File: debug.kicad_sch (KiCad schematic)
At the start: 80 parts, among them J8 USB4105-GF-A, J9 0878311420, Q10 DTC014TEBTL, Q11 DTC014TEBTL, Q12 DTC014TEBTL, U37 WE-TVS-82400152, U38 MIC5211-3.3YM6-TR, U39 93LC66BT-IMC, U40 FT4232HPQ, U41 TPD4E05U06QDQARQ1_PASS, U42 74AVC4T245RSVRG4, U43 74AVC4T245RSVRG4, U44 SN74AVC2T245RSWR, U45 SN74AVC2T245RSWR, U46 NC7WZ07P6X, Y7 ABM8G-12.000MHZ-18-D2Y-T

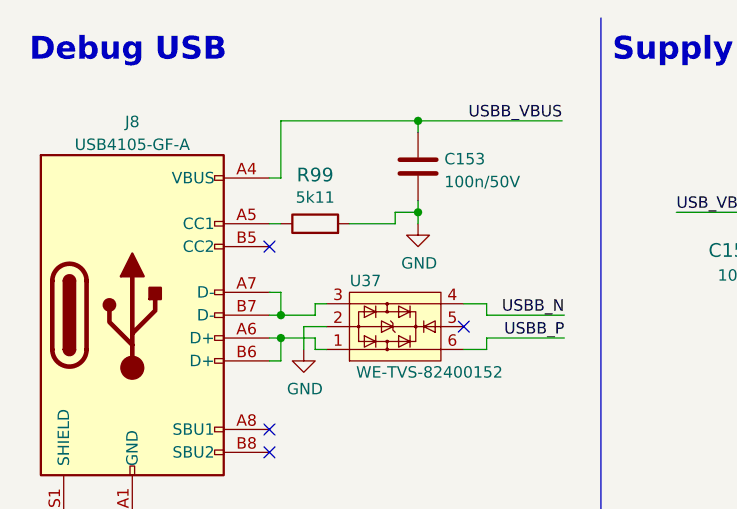
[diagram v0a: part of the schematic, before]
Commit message: Add CC2 5K1 pulldown
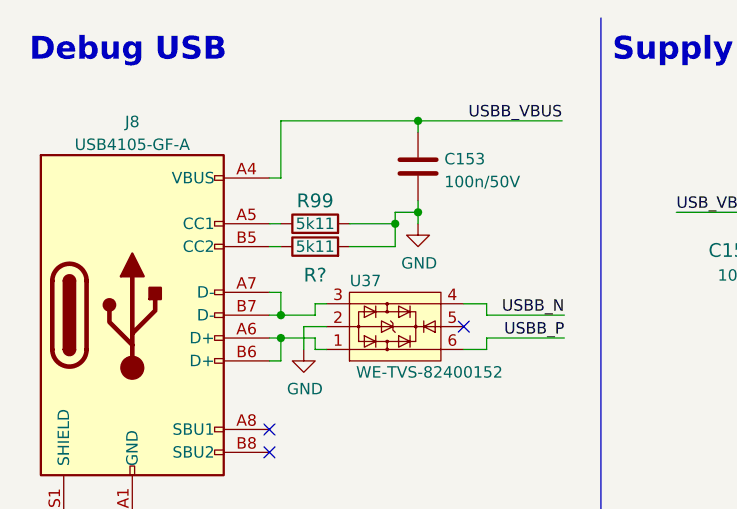
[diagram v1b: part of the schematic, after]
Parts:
- added R?: R_5k11_0402, kria-k26-devboard-footprints:0402-res, symbol kria-k26-devboard:R_5k11_0402
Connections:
- net GND: now also R?.2
- net at J8.B5 (CC2): now also R?.1
- no-connect marks 37 -> 36
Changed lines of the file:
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@@
   (junction (at 53.34 100.33) (diameter 0) (color 0 0 0 0)
   )
+  (junction (at 54.61 35.56) (diameter 0) (color 0 0 0 0)
+  )
   (junction (at 290.83 135.89) (diameter 0) (color 0 0 0 0)
   )
@@
   (no_connect (at 227.33 187.96))
   (no_connect (at 40.64 60.96))
-  (no_connect (at 40.64 38.1))
   (no_connect (at 326.39 66.04))
   (no_connect (at 227.33 149.86))
@@
     (stroke (width 0) (type default) (color 0 0 0 0))
   )
+  (wire (pts (xy 40.64 38.1) (xy 41.91 38.1))
+    (stroke (width 0) (type default) (color 0 0 0 0))
+  )
   (wire (pts (xy 40.64 101.6) (xy 40.64 100.33))
     (stroke (width 0) (type default) (color 0 0 0 0))
@@
     (stroke (width 0) (type default) (color 0 0 0 0))
   )
+  (wire (pts (xy 49.53 38.1) (xy 54.61 38.1))
+    (stroke (width 0) (type default) (color 0 0 0 0))
+  )
   (polyline (pts (xy 299.72 234.95) (xy 299.72 252.73))
     (stroke (width 0) (type default) (color 0 0 0 0))
@@
     (stroke (width 0) (type default) (color 0 0 0 0))
   )
+  (wire (pts (xy 54.61 38.1) (xy 54.61 35.56))
+    (stroke (width 0) (type default) (color 0 0 0 0))
+  )
   (wire (pts (xy 41.91 45.72) (xy 40.64 45.72))
     (stroke (width 0) (type default) (color 0 0 0 0))
@@
   (symbol (lib_id "kria-k26-devboard:R_5k11_0402") (at 45.72 35.56 0) (unit 1)
     (in_bom yes) (on_board yes)
-    (property "Reference" "R99" (id 0) (at 45.72 30.1498 0)
+    (property "Reference" "R99" (id 0) (at 45.72 33.02 0)
       (effects (font (size 1.524 1.524)))
     )
@@
       (effects (font (size 1.524 1.524)) (justify left) hide)
     )
-    (property "Val" "5k11" (id 6) (at 45.72 32.639 0))
+    (property "Val" "5k11" (id 6) (at 45.72 35.56 0))
     (pin "1")
     (pin "2")
@@
     (pin "9")
   )
+  (symbol (lib_id "kria-k26-devboard:R_5k11_0402") (at 45.72 38.1 0) (unit 1)
+    (in_bom yes) (on_board yes)
+    (property "Reference" "R?" (id 0) (at 45.72 41.275 0)
+      (effects (font (size 1.524 1.524)))
+    )
+    (property "Value" "R_5k11_0402" (id 1) (at 45.72 41.91 0)
+      (effects (font (size 1.524 1.524)) hide)
+    )
+    (property "Footprint" "kria-k26-devboard-footprints:0402-res" (id 2) (at 50.8 33.02 0)
+      (effects (font (size 1.524 1.524)) (justify left) hide)
+    )
+    (property "Datasheet" "" (id 3) (at 45.72 38.1 0)
+      (effects (font (size 1.27 1.27)) hide)
+    )
+    (property "Manufacturer" "WALSIN" (id 4) (at 50.8 27.94 0)
+      (effects (font (size 1.524 1.524)) (justify left) hide)
+    )
+    (property "MPN" "WR04X5111FTL" (id 5) (at 50.8 30.48 0)
+      (effects (font (size 1.524 1.524)) (justify left) hide)
+    )
+    (property "Val" "5k11" (id 6) (at 45.72 38.1 0))
+    (pin "1")
+    (pin "2")
+  )
 )

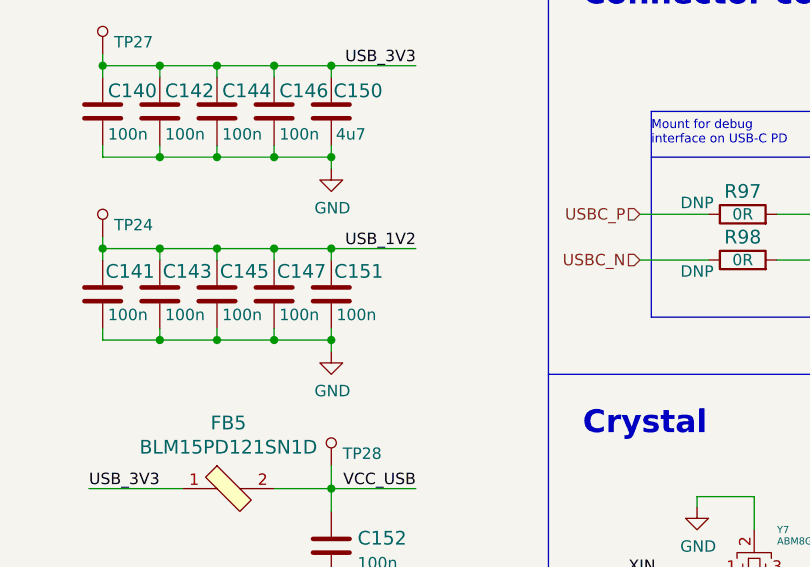
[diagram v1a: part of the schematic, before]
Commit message: Added 4u7 to FTDI Vregout
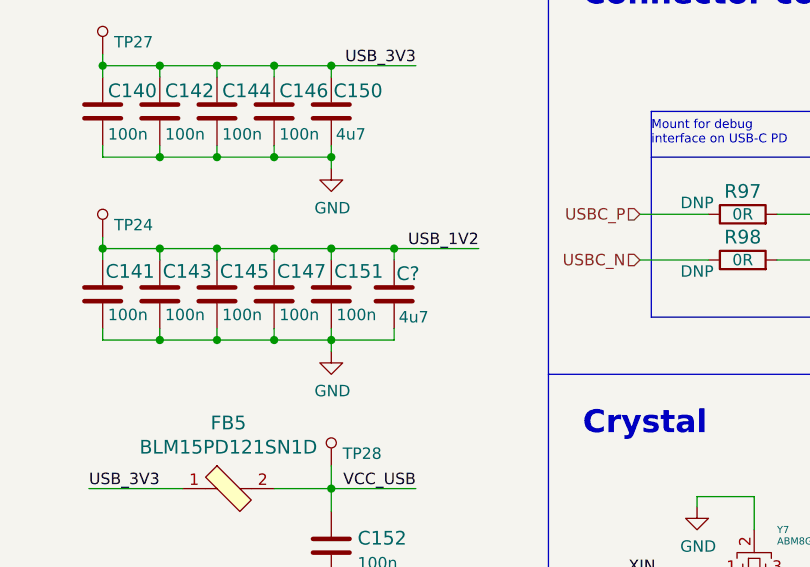
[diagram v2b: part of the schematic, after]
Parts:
- added C?: C_4u7_0402, kria-k26-devboard-footprints:0402-cap, symbol kria-k26-devboard:C_4u7_0402
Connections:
- net GND: now also C?.2
- net USB_1V2: now also C?.1
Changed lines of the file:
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@@
     (comment 2 "Antmicro Ltd.")
   )
+  (junction (at 60.325 120.65) (diameter 0) (color 0 0 0 0)
+  )
   (junction (at 131.318 261.62) (diameter 0) (color 0 0 0 0)
   )
@@
     (stroke (width 0) (type default) (color 0 0 0 0))
   )
+  (wire (pts (xy 53.34 130.81) (xy 60.325 130.81))
+    (stroke (width 0) (type default) (color 0 0 0 0))
+  )
   (wire (pts (xy 153.67 55.88) (xy 166.37 55.88))
     (stroke (width 0) (type default) (color 0 0 0 0))
@@
     (stroke (width 0) (type default) (color 0 0 0 0))
   )
-  (wire (pts (xy 62.738 120.65) (xy 53.34 120.65))
+  (wire (pts (xy 69.723 120.65) (xy 60.325 120.65))
     (stroke (width 0) (type default) (color 0 0 0 0))
   )
@@
     (stroke (width 0) (type default) (color 0 0 0 0))
   )
+  (wire (pts (xy 60.325 120.65) (xy 53.34 120.65))
+    (stroke (width 0) (type default) (color 0 0 0 0))
+  )
   (wire (pts (xy 327.66 114.3) (xy 332.74 114.3))
     (stroke (width 0) (type default) (color 0 0 0 0))
@@
     (stroke (width 0) (type default) (color 0 0 0 0))
   )
+  (wire (pts (xy 60.325 120.65) (xy 60.325 121.92))
+    (stroke (width 0) (type default) (color 0 0 0 0))
+  )
   (polyline (pts (xy 299.72 234.95) (xy 299.72 252.73))
     (stroke (width 0) (type default) (color 0 0 0 0))
@@
     (stroke (width 0) (type default) (color 0 0 0 0))
   )
+  (wire (pts (xy 60.325 130.81) (xy 60.325 129.54))
+    (stroke (width 0) (type default) (color 0 0 0 0))
+  )
   (wire (pts (xy 278.13 259.08) (xy 280.67 259.08))
     (stroke (width 0) (type default) (color 0 0 0 0))
@@
     (effects (font (size 1.27 1.27)) (justify left bottom))
   )
-  (label "USB_1V2" (at 62.738 120.65 180)
+  (label "USB_1V2" (at 69.723 120.65 180)
     (effects (font (size 1.27 1.27)) (justify right bottom))
   )
@@
     (pin "1")
     (pin "2")
+  )
+  (symbol (lib_id "kria-k26-devboard:C_4u7_0402") (at 60.325 125.73 0) (unit 1)
+    (in_bom yes) (on_board yes)
+    (property "Reference" "C?" (id 0) (at 60.579 123.444 0)
+      (effects (font (size 1.524 1.524)) (justify left))
+    )
+    (property "Value" "C_4u7_0402" (id 1) (at 60.325 129.54 0)
+      (effects (font (size 1.524 1.524)) hide)
+    )
+    (property "Footprint" "kria-k26-devboard-footprints:0402-cap" (id 2) (at 65.405 120.65 0)
+      (effects (font (size 1.524 1.524)) (justify left) hide)
+    )
+    (property "Datasheet" "" (id 3) (at 60.325 125.73 0)
+      (effects (font (size 1.27 1.27)) hide)
+    )
+    (property "Manufacturer" "MURATA" (id 4) (at 65.405 115.57 0)
+      (effects (font (size 1.524 1.524)) (justify left) hide)
+    )
+    (property "MPN" "GRM155R61A475MEAAD" (id 5) (at 65.405 118.11 0)
+      (effects (font (size 1.524 1.524)) (justify left) hide)
+    )
+    (property "Val" "4u7" (id 6) (at 60.833 128.27 0)
+      (effects (font (size 1.27 1.27)) (justify left))
+    )
+    (pin "1")
+    (pin "2")

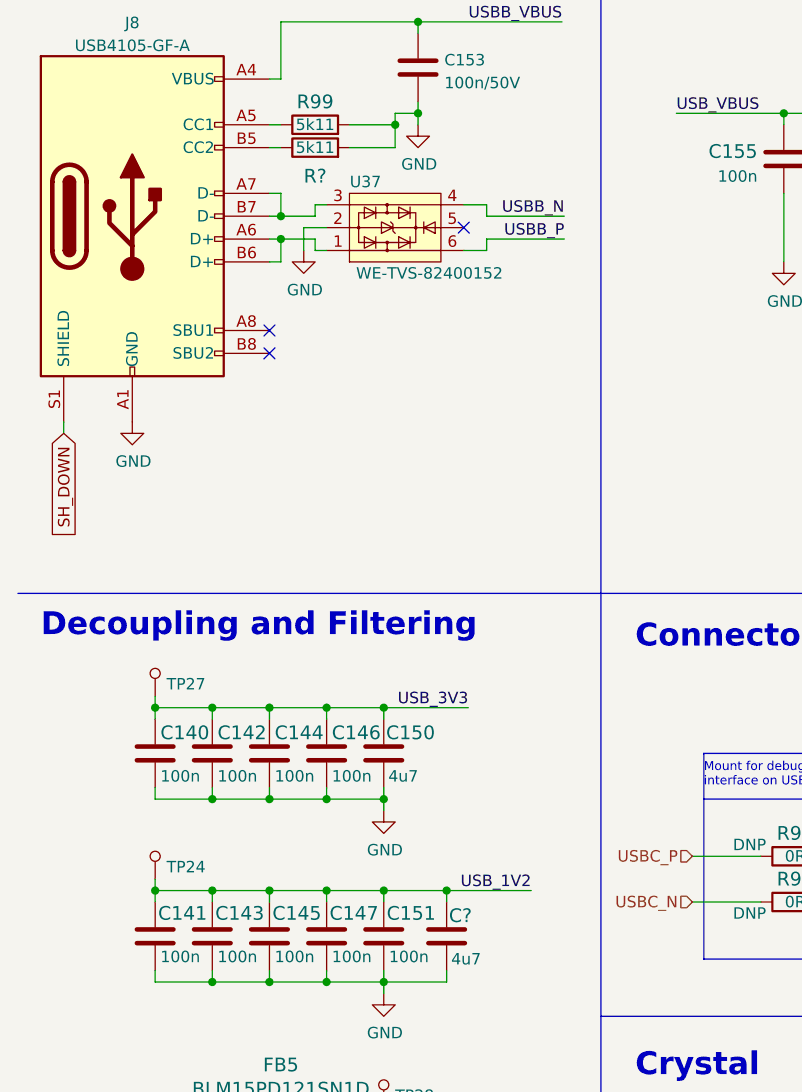
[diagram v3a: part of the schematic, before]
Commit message: Add decoupling to cammera and DP connector, schematic cleanup
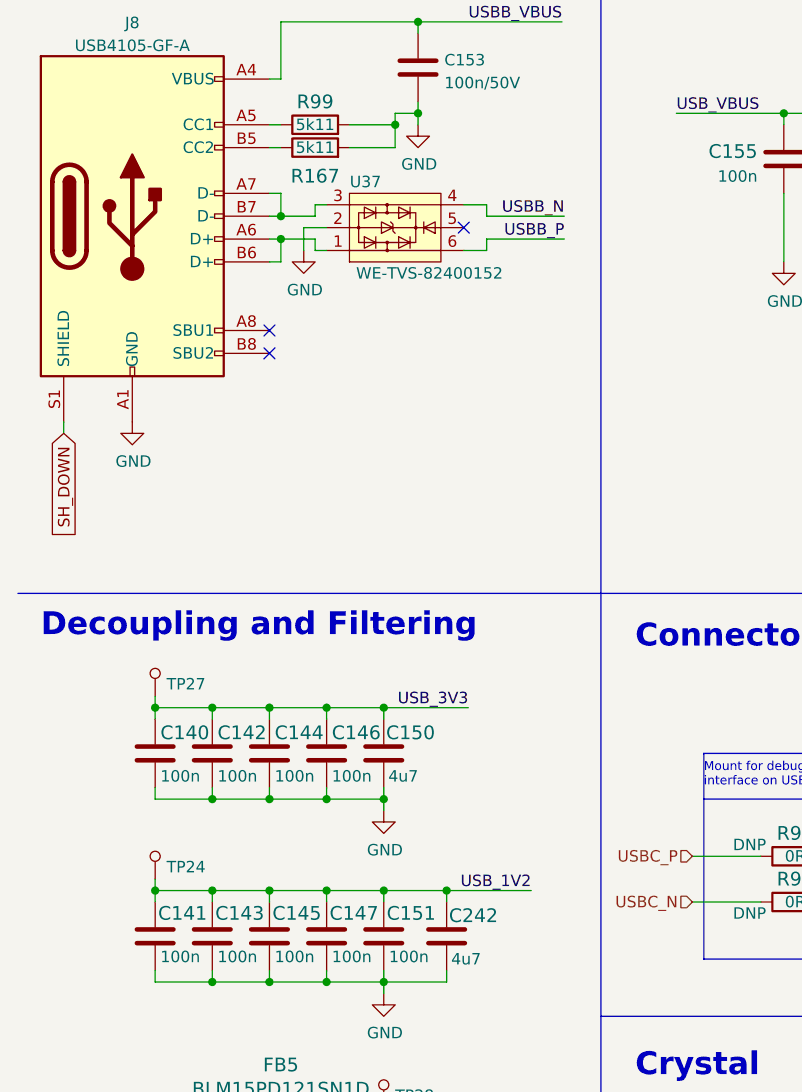
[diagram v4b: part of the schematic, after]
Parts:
- gave numbers to parts that had none: 2
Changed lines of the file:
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@@
   (symbol (lib_id "kria-k26-devboard:R_5k11_0402") (at 45.72 38.1 0) (unit 1)
     (in_bom yes) (on_board yes)
-    (property "Reference" "R?" (id 0) (at 45.72 41.275 0)
+    (property "Reference" "R167" (id 0) (at 45.72 41.275 0)
       (effects (font (size 1.524 1.524)))
     )
@@
   (symbol (lib_id "kria-k26-devboard:C_4u7_0402") (at 60.325 125.73 0) (unit 1)
     (in_bom yes) (on_board yes)
-    (property "Reference" "C?" (id 0) (at 60.579 123.444 0)
+    (property "Reference" "C242" (id 0) (at 60.579 123.444 0)
       (effects (font (size 1.524 1.524)) (justify left))
     )

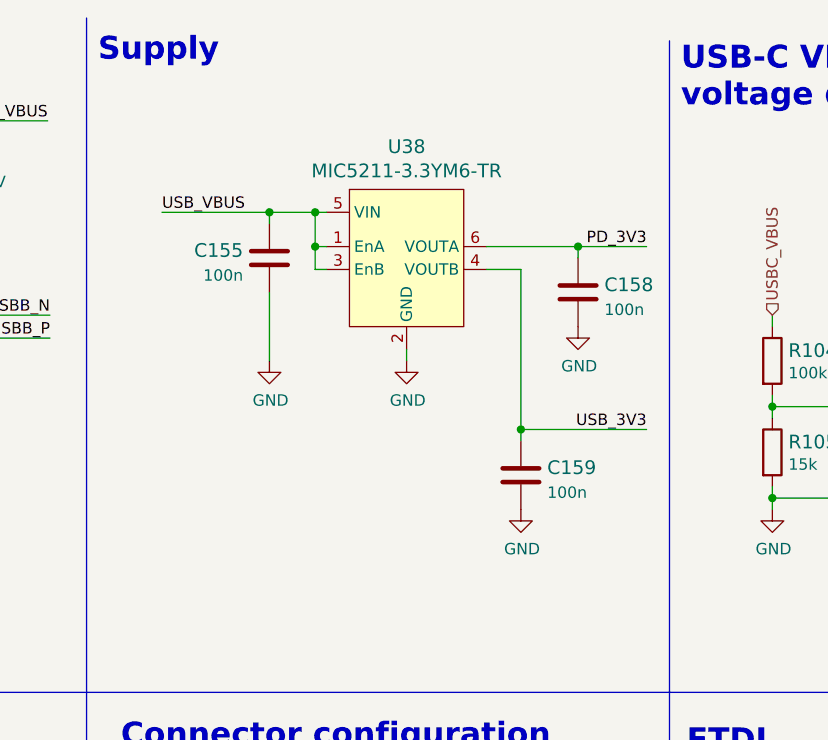
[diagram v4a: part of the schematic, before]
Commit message: Replace FTDI 3V3 Regulator
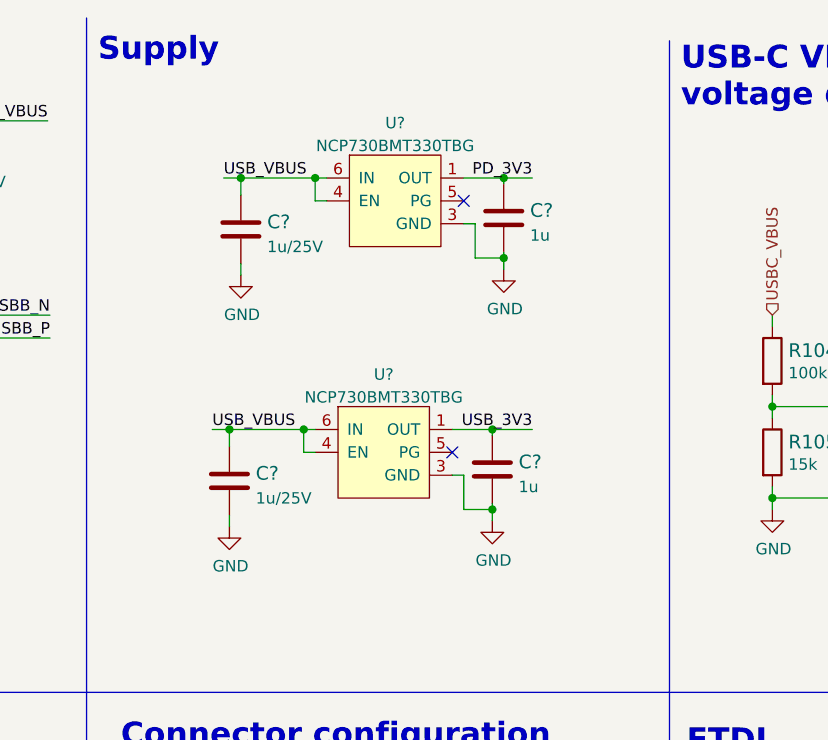
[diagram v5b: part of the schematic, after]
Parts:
- removed C155, C158, C159: C_100n_0402, kria-k26-devboard-footprints:0402-cap, symbol kria-k26-devboard:C_100n_0402
- removed U38: MIC5211-3.3YM6-TR, kria-k26-devboard-footprints:SOT-23-6, symbol kria-k26-devboard:MIC5211-3.3YM6-TR
- added C? (x2): C_1u_0402, antmicro-footprints:0402-cap, symbol antmicroCapacitors0402:C_1u_0402
- added C? (x2): C_1u_0603_25V, antmicro-footprints:0603-cap, symbol antmicroCapacitors0603:C_1u_0603_25V
- added U? (x2): NCP730BMT330TBG, antmicro-footprints:WSON6_TI_2x2mm, symbol antmicroPMICVoltageRegulatorsLinear:NCP730BMT330TBG
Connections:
- net GND: now also C?.2, C?.2, C?.2, C?.2, U?.3 (GND), U?.3 (GND), U?.7 (EP), U?.7 (EP)
- net PD_3V3: now also C?.1, U?.1 (OUT)
- net USB_3V3: now also C?.1, U?.1 (OUT)
- net USB_VBUS: now also C?.1, C?.1, U?.4 (EN), U?.4 (EN), U?.6 (IN), U?.6 (IN)
- no-connect marks 36 -> 38

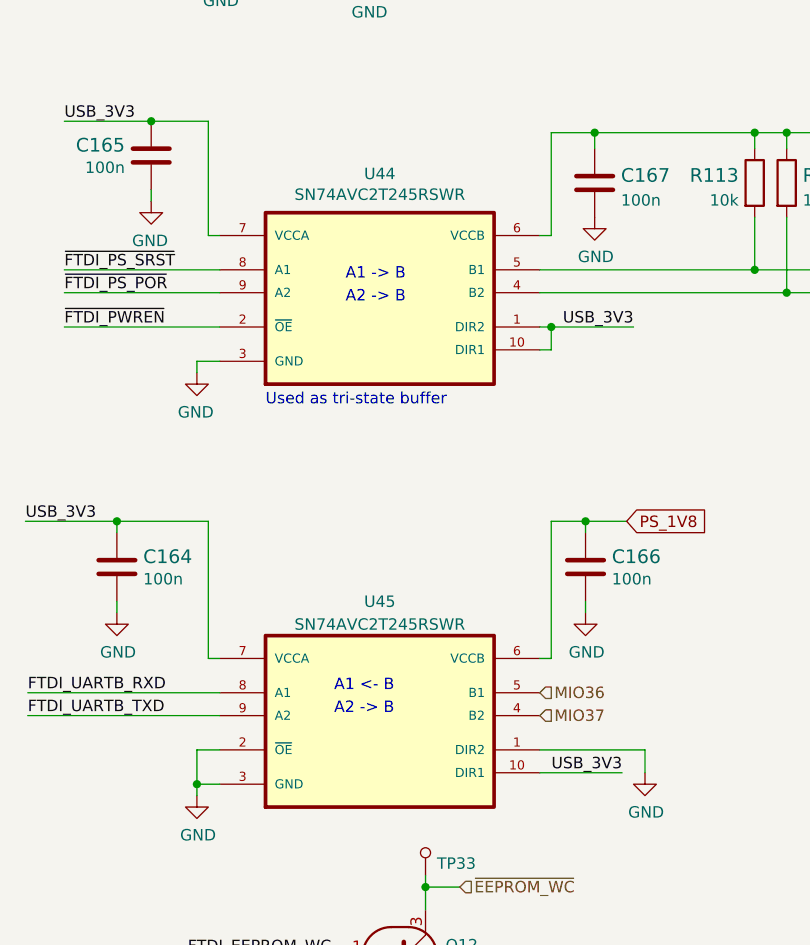
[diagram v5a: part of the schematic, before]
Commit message: Fix SN74AVC2T245RSWR symbol and cross on U45
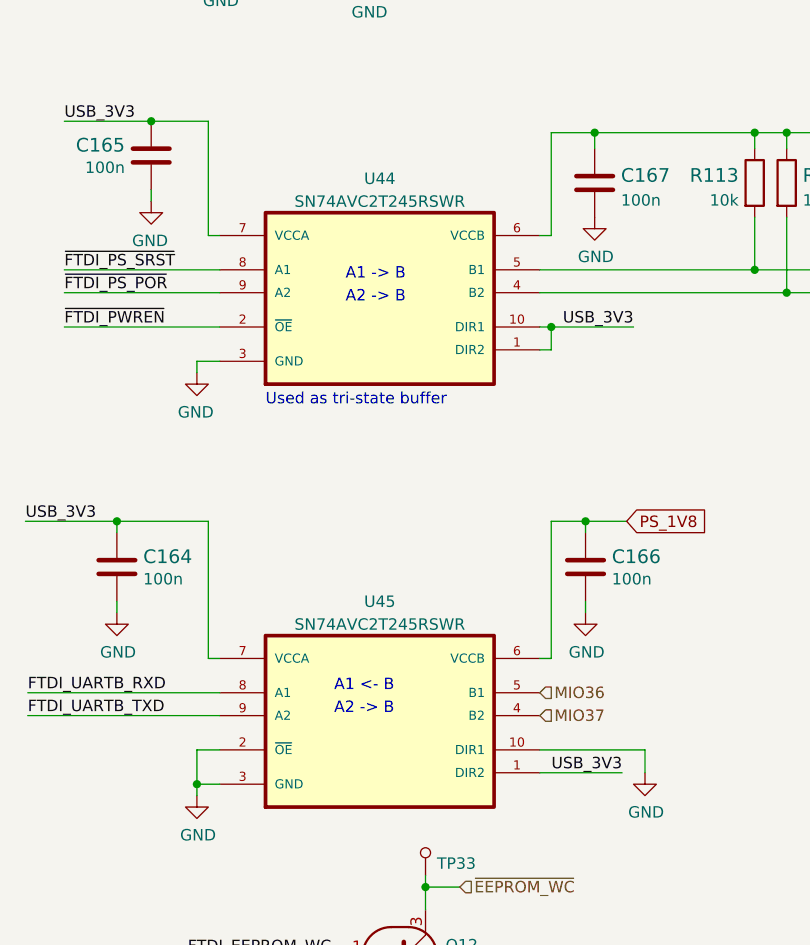
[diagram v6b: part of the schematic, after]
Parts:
- removed U44, U45: SN74AVC2T245RSWR, kria-k26-devboard-footprints:Texas_RSW0010A, symbol kria-k26-devboard:SN74AVC2T245RSWR
- added U44, U45: SN74AVC2T245RSWR, antmicro-footprints:Texas_RSW0010A, symbol antmicroLogicTranslatorsLevelShifters:SN74AVC2T245RSWR
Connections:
- net FTDI_UARTB_RXD: now also U45.8 (A1)
- net FTDI_UARTB_TXD: now also U45.9 (A2)
- net GND: now also U44.3 (GND), U45.10 (DIR1), U45.2 (~{OE}), U45.3 (GND)
- net MIO36: now also U45.5 (B1)
- net MIO37: now also U45.4 (B2)
- net PS_1V8: now also U45.6 (VCCB)
- net USB_3V3: now also U44.1 (DIR2), U44.10 (DIR1), U44.6 (VCCB), U44.7 (VCCA), U45.1 (DIR2), U45.7 (VCCA)
- net ~{FTDI_PS_POR}: now also U44.9 (A2)
- net ~{FTDI_PS_SRST}: now also U44.8 (A1)
- net ~{FTDI_PWREN}: now also U44.2 (~{OE})
- net at R113.2, U46.1 (A1): now also U44.5 (B1)
- net at R114.2, U46.3 (A2): now also U44.4 (B2)
